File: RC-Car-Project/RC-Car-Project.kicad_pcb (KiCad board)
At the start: 4 copper layers, 80 x 120 mm, 142 parts, among them J1 Conn_01x02_Pin, J10 ANT_IF, J11 Conn_01x02, J12 Conn_01x02, J13 RF_IF, J15 USB4120-03-C_REVA, J2 Conn_01x02_Pin, J3 Conn_01x02_Pin, J4 Conn_01x02_Pin, J5 MCU_IF, J6 Conn_01x02, J7 Conn_01x02, J8 Conn_01x02, J9 Conn_02x09_Odd_Even, Q1 BTN8982TA, Q2 BTN8982TA, Q3 BTN8982TA, Q4 BTN8982TA, Q5 2N7002E, Q6 2N7002E, Q7 PMOS, SW1 SW_Push, U1 LMR16020PDDAR, U11 LMR16030PDDA, U3 STM32H743VGTx, U4 USBLC6-2SC6, U7 INA229AQDGSRQ1, U8 ADC082S021CIMM/NOPB, U9 SN74HC244PWR, Y1 Crystal

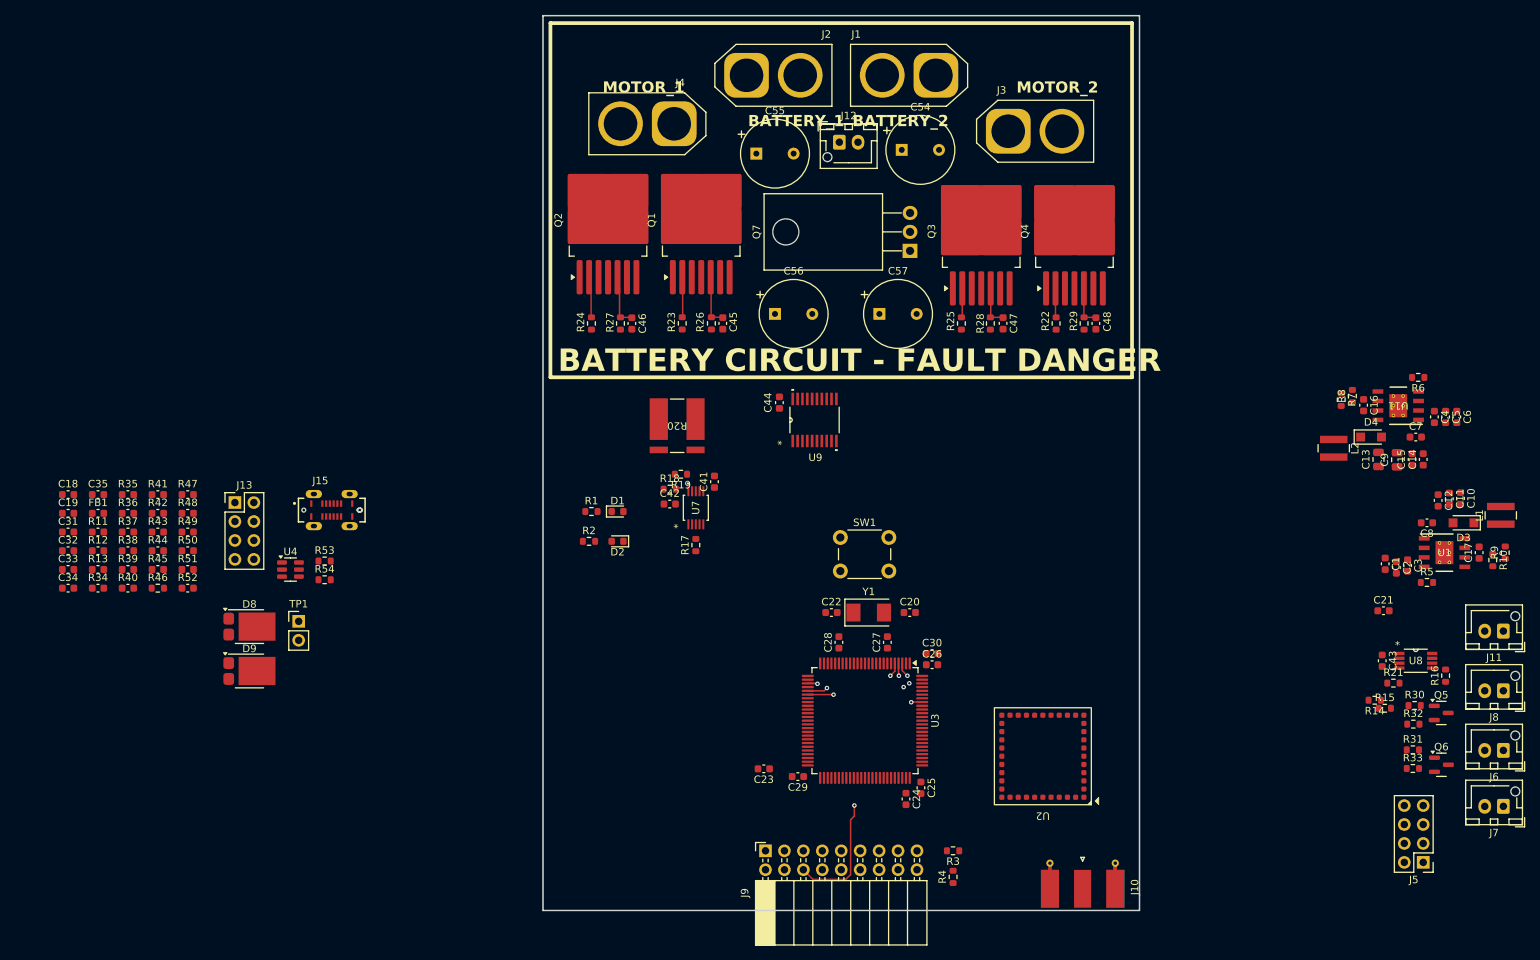
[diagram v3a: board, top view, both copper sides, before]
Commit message: Routed SDIO/DCMI with imp. matching and length matching
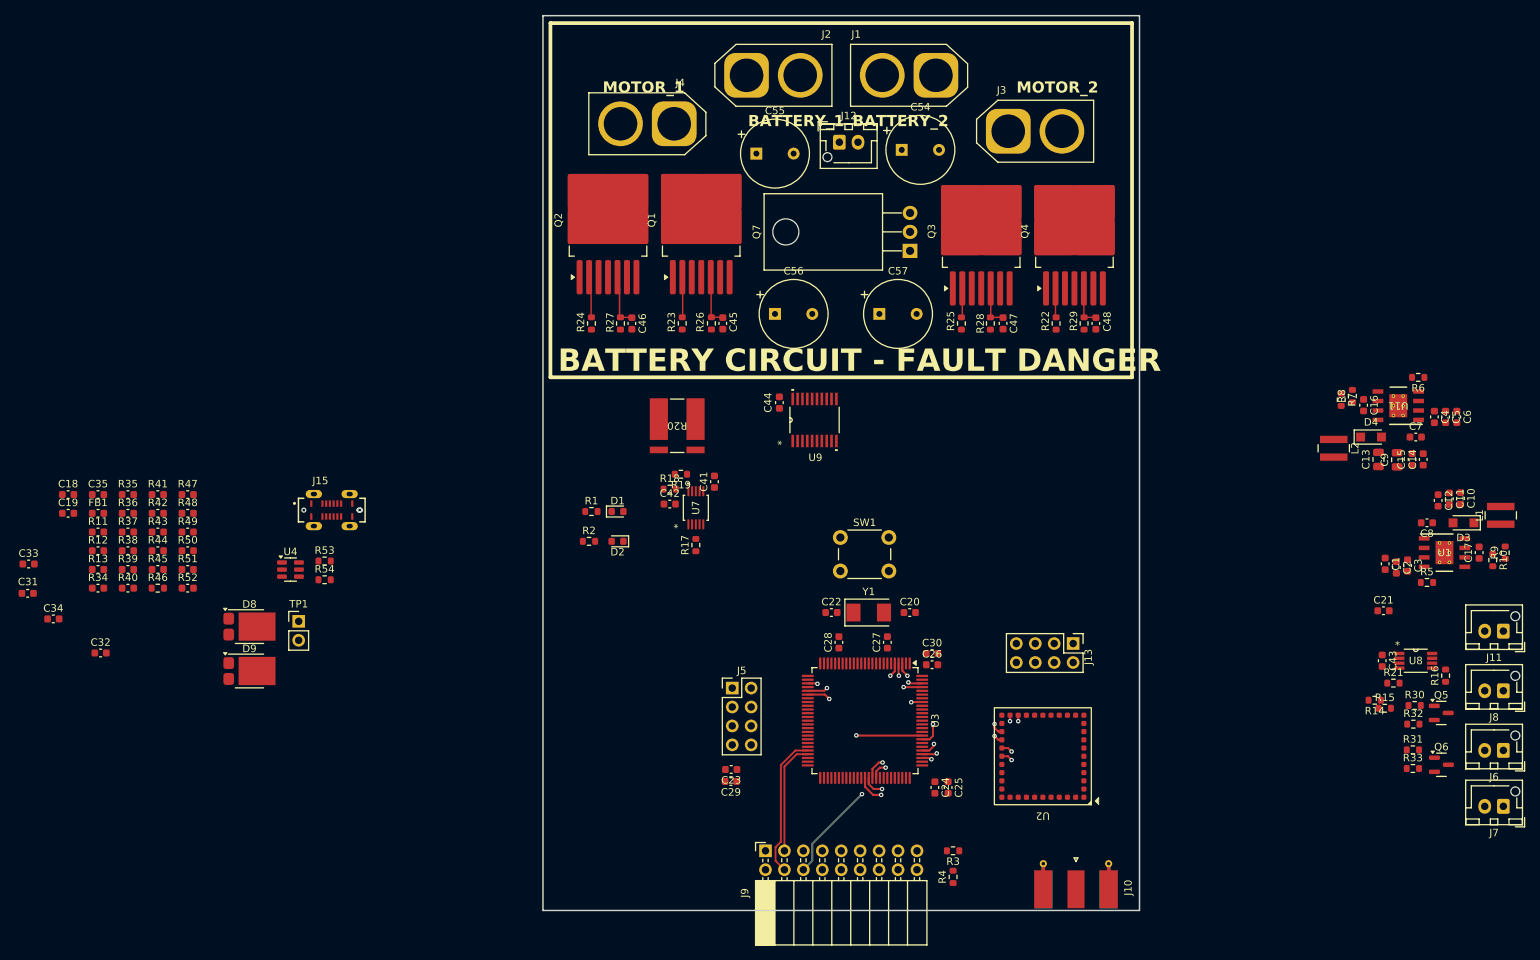
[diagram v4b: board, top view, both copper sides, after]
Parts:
- moved J13 114.0 mm to (181.1, 124.2), turned to -90 degrees
- moved J5 95.6 mm to (135.4, 130.2), turned to 0 degrees
- moved C32 14.4 mm to (50.7, 125.5)
- moved C31 9.85 mm to (40.9, 117.5)
- moved C29 9.01 mm to (135.2, 142.7)
- moved C33 5.35 mm to (41.0, 113.5)
- moved C34 4.58 mm to (44.3, 120.9)
- moved C23 4.37 mm to (135.2, 141.1)
- moved C24 4.17 mm to (162.6, 143.5)
- moved C25 3.65 mm to (164.3, 143.5)
- moved J10 0.89 mm to (181.5, 155.4)
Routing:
- net /MCU/SDMMC1_CMD: track 0.00 -> 24.1 mm, vias 0 -> 2
- net /MCU/SDMMC1_CK: track 0.00 -> 23.2 mm, vias 0 -> 2
- net /MCU/SDMMC1_D0: track 0.00 -> 22.6 mm, vias 0 -> 2
- net /MCU/SDMMC1_D2: track 0.00 -> 22.2 mm, vias 0 -> 2
- net /MCU/SDMMC1_D3: track 0.00 -> 22.0 mm, vias 0 -> 2
- net /MCU/SDMMC1_D1: track 0.00 -> 21.5 mm, vias 0 -> 2
- net /Connectors/DCMI_D0: track 9.96 -> 30.0 mm, vias 0 -> 1
- net /Connectors/DCMI_D1: track 13.9 -> 30.1 mm, vias 0 -> 1
- net /Connectors/DCMI_D5: track 21.8 -> 30.2 mm, vias 0 -> 1
- net /Connectors/DCMI_VSYNC: track 35.9 -> 29.9 mm
- net /Connectors/DCMI_HSYNC: track 25.1 -> 30.1 mm
- net /Connectors/DCMI_XCLK: track 25.6 -> 30.1 mm
- net /Connectors/DCMI_D2: track 28.0 -> 30.2 mm
- net /Connectors/DCMI_D6: track 29.0 -> 30.3 mm
- net /Connectors/DCMI_PIXCLK: track 28.9 -> 30.2 mm
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
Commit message: Laid out 3V3 section of Tank PCB
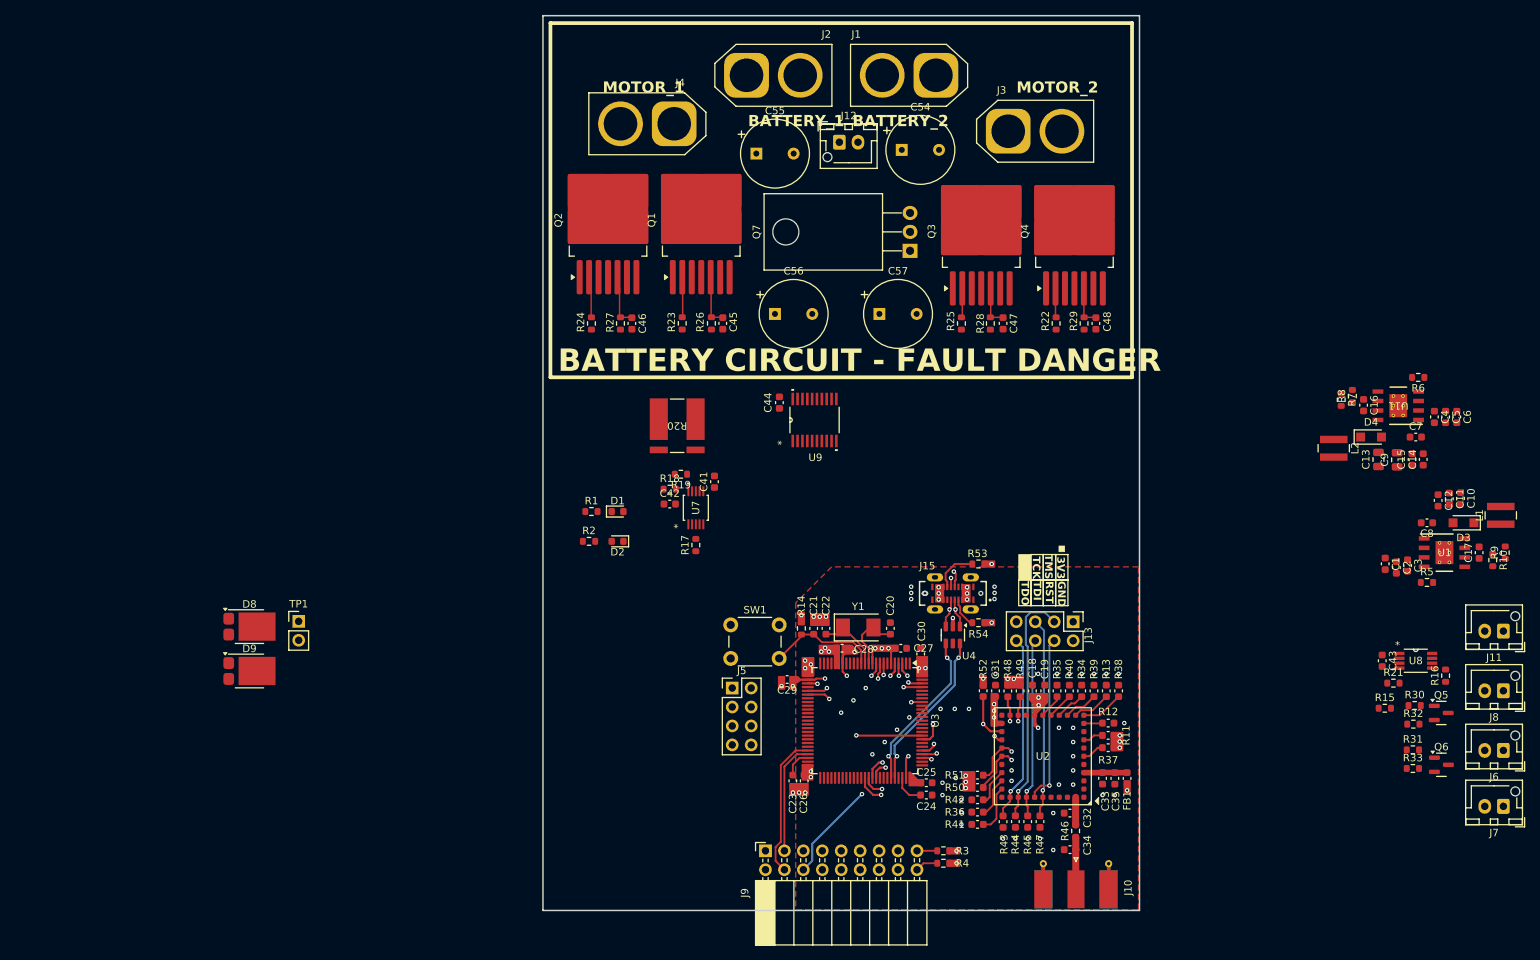
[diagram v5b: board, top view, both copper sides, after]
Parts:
- moved C33 146.9 mm to (185.0, 142.3), turned to -90 degrees
- moved FB1 142.5 mm to (188.3, 142.3), turned to 90 degrees
- moved C35 141.6 mm to (186.7, 142.3), turned to -90 degrees
- moved C34 139.8 mm to (180.7, 151.8), turned to 180 degrees
- moved R11 138.2 mm to (185.8, 136.5)
- moved R12 137.4 mm to (185.8, 134.9)
- moved R13 136.2 mm to (185.5, 130.6), turned to 90 degrees
- moved R37 134.6 mm to (185.8, 138.2)
- moved R38 134.2 mm to (187.2, 130.6), turned to 90 degrees
- moved C19 133.1 mm to (177.3, 130.6), turned to 90 degrees
- moved R34 132.6 mm to (182.2, 130.6), turned to 90 degrees
- moved C18 132.0 mm to (175.6, 130.6), turned to 90 degrees
- moved C32 131.8 mm to (180.7, 146.9), turned to 180 degrees
- moved R39 130.6 mm to (183.9, 130.6), turned to 90 degrees
- moved C31 130.5 mm to (170.7, 130.6), turned to 90 degrees
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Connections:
- U4 pad 1: Net-(J15-D1-) -> Net-(J15-D1+)
- U4 pad 3: Net-(J15-D1+) -> Net-(J15-D1-)
- U4 pad 4: /Connectors/CON_USB_D+ -> /Connectors/CON_USB_D-
- U4 pad 6: /Connectors/CON_USB_D- -> /Connectors/CON_USB_D+
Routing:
- net /Connectors/RF_TMS: track 0.00 -> 32.0 mm, vias 0 -> 1
- net /Connectors/RF_TCK: track 0.00 -> 26.7 mm, vias 0 -> 1
- net /Connectors/RF_TDO: track 0.00 -> 25.0 mm, vias 0 -> 1
- net /Connectors/RF_TDI: track 0.00 -> 24.2 mm, vias 0 -> 1
- net /Connectors/RF_nTRST: track 0.00 -> 22.8 mm, vias 0 -> 1
- net /Connectors/CON_USB_D-: track 0.00 -> 21.9 mm, vias 0 -> 2
- net /Connectors/CON_USB_D+: track 0.00 -> 21.9 mm, vias 0 -> 2
- net /Connectors/NRST: track 0.00 -> 15.2 mm
- net +3V3: track 0.00 -> 13.0 mm, vias 0 -> 30
- net Net-(J15-D1-): track 0.00 -> 12.0 mm, vias 0 -> 2
- net Net-(J15-D1+): track 0.00 -> 12.0 mm, vias 0 -> 2
- net GNDA: track 0.00 -> 9.72 mm, vias 0 -> 66
- net /MCU/OSC_IN: track 0.00 -> 8.79 mm
- net /MCU/OSC_OUT: track 0.00 -> 8.72 mm
- net /Connectors/RF_ANT: track 0.00 -> 7.01 mm
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- added copper zone on In1.Cu, net +3V3
- added copper zone on F.Cu, net GNDA
- added copper zone on In2.Cu, net GNDA
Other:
- board text added: "3V3 TMS TCK"
- board text added: "GND RST TDI TDO"

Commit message: Changed
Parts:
- removed C54, C55: C_Polarized, Capacitor_THT:CP_Radial_Tantal_D9.0mm_P5.00mm
- C56, C57: footprint Capacitor_THT:CP_Radial_Tantal_D9.0mm_P5.00mm -> Capacitor_THT:CP_Radial_D10.0mm_P5.00mm
- moved J7 126.0 mm to (115.1, 122.2), turned to 0 degrees
- moved J11 125.9 mm to (115.1, 145.7), turned to 0 degrees
- moved J6 124.1 mm to (115.1, 129.7), turned to 0 degrees
- moved J8 123.9 mm to (115.1, 137.7), turned to 0 degrees
- moved R16 108.8 mm to (122.8, 139.7), turned to -90 degrees
- moved Q6 107.9 mm to (123.4, 127.7), turned to 180 degrees
- moved Q5 107.1 mm to (123.4, 134.7), turned to 180 degrees
- moved U8 101.4 mm to (126.8, 141.7), turned to 180 degrees
- moved R33 100.4 mm to (127.2, 127.2), turned to 180 degrees
- moved R30 100.0 mm to (127.0, 135.7), turned to 180 degrees
- moved R31 99.8 mm to (127.2, 129.7), turned to 180 degrees
- moved R32 99.6 mm to (127.1, 133.2), turned to 180 degrees
- moved R21 94.7 mm to (129.8, 138.7), turned to 180 degrees
- moved C43 92.5 mm to (131.3, 141.7), turned to 90 degrees
- moved R15 92.0 mm to (131.0, 135.3), turned to 180 degrees
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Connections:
- U9 pad 16: Net-(Q2-IN) -> Net-(Q1-IN)
- U9 pad 18: Net-(Q1-IN) -> Net-(Q2-IN)
- U9 pad 2: /MCU/LEFT_PWM1 -> /MCU/RIGHT_PWM1
- U9 pad 4: /MCU/RIGHT_PWM1 -> /MCU/LEFT_PWM1
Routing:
- net /IVTSense/SCLK: track 0.00 -> 55.0 mm, vias 0 -> 2
- net /Connectors/SWCLK: track 0.00 -> 50.6 mm, vias 0 -> 1
- net Net-(Q2-IN): track 3.90 -> 49.9 mm, vias 0 -> 2
- net /Connectors/SWDIO: track 0.00 -> 37.2 mm, vias 0 -> 1
- net Net-(Q1-IN): track 3.89 -> 40.7 mm, vias 0 -> 2
- net +3V3: track 13.0 -> 48.6 mm, vias 30 -> 42
- net /Connectors/USART_TX: track 0.00 -> 32.5 mm, vias 0 -> 1
- net /IVTSense/ALERT: track 0.00 -> 32.3 mm, vias 0 -> 2
- net /IVTSense/MISO: track 0.00 -> 32.3 mm, vias 0 -> 2
- net /Connectors/USART_RX: track 0.00 -> 29.0 mm, vias 0 -> 1
- net /IVTSense/MOSI: track 0.00 -> 28.7 mm, vias 0 -> 2
- net /IVTSense/INA_CS: track 2.13 -> 30.5 mm, vias 1 -> 2
- net Net-(Q4-IN): track 3.91 -> 31.4 mm, vias 0 -> 2
- net Net-(Q3-IN): track 3.93 -> 24.8 mm, vias 0 -> 2
- net VDD_BATT: track 0.00 -> 19.7 mm, vias 0 -> 70
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- added copper zone on F.Cu, net GND_BATT
- added copper zone on B.Cu, net VDD_BATT
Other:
- board text added: "RX DIO GND"
- board text added: "TX CLK RST 3V3"
